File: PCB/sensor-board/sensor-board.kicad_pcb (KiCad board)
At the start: 2 copper layers, 70 x 58 mm, 37 parts, among them J1 SENSOR, Q1 BSS138, Q2 BSS138, Q3 BSS138, Q4 BSS138

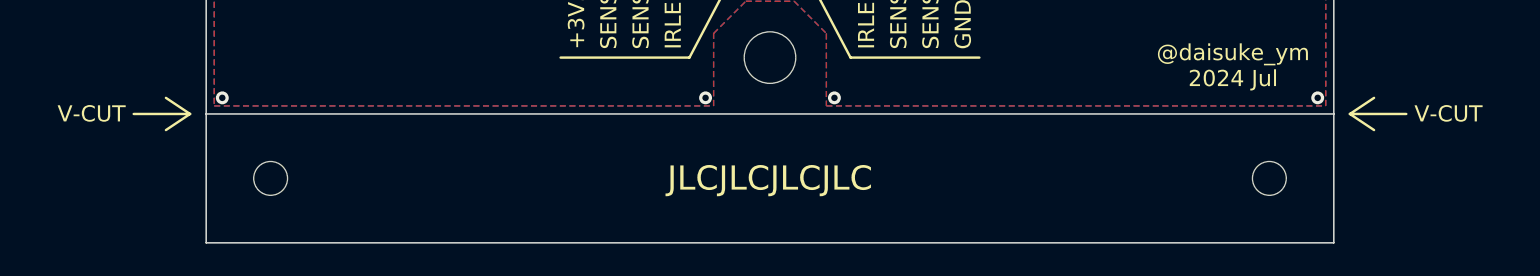
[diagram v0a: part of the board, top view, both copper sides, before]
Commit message: JLCPCB で監査エラー（V-CUTできるサイズを超えているとのこと）が出たので、マウスバイトに変更した。
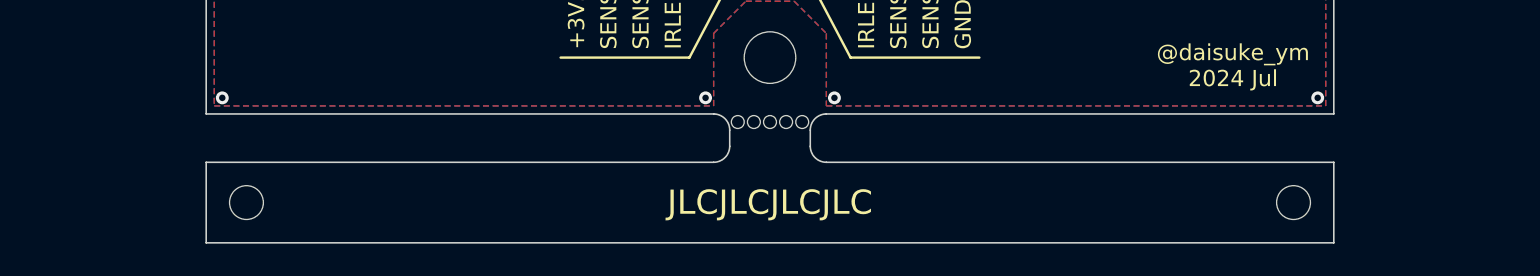
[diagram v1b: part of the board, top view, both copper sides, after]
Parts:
- added CH**: CuttingHole_0.8, MyLib:CuttingHole_0.8, F.Cu at (151.0, 92.5)
- added CH**: CuttingHole_0.8, MyLib:CuttingHole_0.8, F.Cu at (149.0, 92.5)
- added CH**: CuttingHole_0.8, MyLib:CuttingHole_0.8, F.Cu at (148.0, 92.5)
- added CH**: CuttingHole_0.8, MyLib:CuttingHole_0.8, F.Cu at (150.0, 92.5)
- added CH**: CuttingHole_0.8, MyLib:CuttingHole_0.8, F.Cu at (152.0, 92.5)
- moved REF** 2.12 mm to (117.5, 97.5)
- moved REF** 2.12 mm to (182.5, 97.5)
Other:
- outline, holes or cut-outs redrawn
- board text removed: "V-CUT"
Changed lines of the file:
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@@
   )
   (footprint "MountingHole:MountingHole_2.1mm" (layer "F.Cu")
-    (at 119 96)
+    (at 117.5 97.5)
     (descr "Mounting Hole 2.1mm, no annular")
     (tags "mounting hole 2.1mm no annular")
@@
       (rotate (xyz 0 0 0))
     )
+  )
+  (footprint "MyLib:CuttingHole_0.8" (layer "F.Cu")
+    (at 151 92.5)
+    (attr through_hole)
+    (fp_text reference "CH**" (at 0 -2 unlocked) (layer "F.SilkS") hide
+        (effects (font (size 1 1) (thickness 0.1)))
+    )
+    (fp_text value "CuttingHole_0.8" (at 0 2.5 unlocked) (layer "F.Fab") hide
+        (effects (font (size 1 1) (thickness 0.15)))
+    )
+    (fp_text user "${REFERENCE}" (at 0 4 unlocked) (layer "F.Fab") hide
+        (effects (font (size 1 1) (thickness 0.15)))
+    )
+    (pad "" np_thru_hole circle (at 0 0) (size 0.8 0.8) (drill 0.8) (layers "F&B.Cu" "*.Mask"))
   )
   (footprint "MountingHole:MountingHole_3.2mm_M3" (layer "F.Cu")
@@
   )
   (footprint "MountingHole:MountingHole_2.1mm" (layer "F.Cu")
-    (at 181 96)
+    (at 182.5 97.5)
     (descr "Mounting Hole 2.1mm, no annular")
     (tags "mounting hole 2.1mm no annular")
@@
       (rotate (xyz 0 0 0))
     )
+  )
+  (footprint "MyLib:CuttingHole_0.8" (layer "F.Cu")
+    (at 149 92.5)
+    (attr through_hole)
+    (fp_text reference "CH**" (at 0 -2 unlocked) (layer "F.SilkS") hide
+        (effects (font (size 1 1) (thickness 0.1)))
+    )
+    (fp_text value "CuttingHole_0.8" (at 0 2.5 unlocked) (layer "F.Fab") hide
+        (effects (font (size 1 1) (thickness 0.15)))
+    )
+    (fp_text user "${REFERENCE}" (at 0 4 unlocked) (layer "F.Fab") hide
+        (effects (font (size 1 1) (thickness 0.15)))
+    )
+    (pad "" np_thru_hole circle (at 0 0) (size 0.8 0.8) (drill 0.8) (layers "F&B.Cu" "*.Mask"))
+  )
+  (footprint "MyLib:CuttingHole_0.8" (layer "F.Cu")
+    (at 148 92.5)
+    (attr through_hole)
+    (fp_text reference "CH**" (at 0 -2 unlocked) (layer "F.SilkS") hide
+        (effects (font (size 1 1) (thickness 0.1)))
+    )
+    (fp_text value "CuttingHole_0.8" (at 0 2.5 unlocked) (layer "F.Fab") hide
+        (effects (font (size 1 1) (thickness 0.15)))
+    )
+    (fp_text user "${REFERENCE}" (at 0 4 unlocked) (layer "F.Fab") hide
+        (effects (font (size 1 1) (thickness 0.15)))
+    )
+    (pad "" np_thru_hole circle (at 0 0) (size 0.8 0.8) (drill 0.8) (layers "F&B.Cu" "*.Mask"))
   )
   (footprint "Capacitor_SMD:C_0805_2012Metric" (layer "F.Cu")
@@
     )
   )
+  (footprint "MyLib:CuttingHole_0.8" (layer "F.Cu")
+    (at 150 92.5)
+    (attr through_hole)
+    (fp_text reference "CH**" (at 0 -2 unlocked) (layer "F.SilkS") hide
+        (effects (font (size 1 1) (thickness 0.1)))
+    )
+    (fp_text value "CuttingHole_0.8" (at 0 2.5 unlocked) (layer "F.Fab") hide
+        (effects (font (size 1 1) (thickness 0.15)))
+    )
+    (fp_text user "${REFERENCE}" (at 0 4 unlocked) (layer "F.Fab") hide
+        (effects (font (size 1 1) (thickness 0.15)))
+    )
+    (pad "" np_thru_hole circle (at 0 0) (size 0.8 0.8) (drill 0.8) (layers "F&B.Cu" "*.Mask"))
+  )
   (footprint "Resistor_SMD:R_0603_1608Metric" (layer "F.Cu")
     (at 175 70 180)
@@
       (rotate (xyz 0 0 0))
     )
+  )
+  (footprint "MyLib:CuttingHole_0.8" (layer "F.Cu")
+    (at 152 92.5)
+    (attr through_hole)
+    (fp_text reference "CH**" (at 0 -2 unlocked) (layer "F.SilkS") hide
+        (effects (font (size 1 1) (thickness 0.1)))
+    )
+    (fp_text value "CuttingHole_0.8" (at 0 2.5 unlocked) (layer "F.Fab") hide
+        (effects (font (size 1 1) (thickness 0.15)))
+    )
+    (fp_text user "${REFERENCE}" (at 0 4 unlocked) (layer "F.Fab") hide
+        (effects (font (size 1 1) (thickness 0.15)))
+    )
+    (pad "" np_thru_hole circle (at 0 0) (size 0.8 0.8) (drill 0.8) (layers "F&B.Cu" "*.Mask"))
   )
   (footprint "MountingHole:MountingHole_3.2mm_M3" (layer "F.Cu")
@@
   (gr_line (start 150 79) (end 145 88.5)
     (stroke (width 0.15) (type default)) (layer "B.SilkS"))
-  (gr_line (start 110.5 92) (end 114 92)
-    (stroke (width 0.15) (type default)) (layer "F.SilkS"))
-  (gr_line (start 186 92) (end 187.5 91)
-    (stroke (width 0.15) (type default)) (layer "F.SilkS"))
-  (gr_line (start 186 92) (end 187.5 93)
-    (stroke (width 0.15) (type default)) (layer "F.SilkS"))
-  (gr_line (start 189.5 92) (end 186 92)
-    (stroke (width 0.15) (type default)) (layer "F.SilkS"))
-  (gr_line (start 114 92) (end 112.5 91)
-    (stroke (width 0.15) (type default)) (layer "F.SilkS"))
   (gr_line (start 163 88.5) (end 155 88.5)
     (stroke (width 0.15) (type default)) (layer "F.SilkS"))
@@
   (gr_line (start 145 88.5) (end 150 79)
     (stroke (width 0.15) (type default)) (layer "F.SilkS"))
-  (gr_line (start 114 92) (end 112.5 93)
-    (stroke (width 0.15) (type default)) (layer "F.SilkS"))
+  (gr_arc (start 147.5 94) (mid 147.207107 94.707107) (end 146.5 95)
+    (stroke (width 0.1) (type default)) (layer "Edge.Cuts"))
   (gr_line (start 142 42) (end 142 63)
     (stroke (width 0.1) (type default)) (layer "Edge.Cuts"))
+  (gr_line (start 146.5 95) (end 115 95)
+    (stroke (width 0.1) (type default)) (layer "Edge.Cuts"))
   (gr_arc (start 158 63) (mid 157.707107 63.707107) (end 157 64)
     (stroke (width 0.1) (type default)) (layer "Edge.Cuts"))
@@
   (gr_line (start 143 64) (end 157 64)
     (stroke (width 0.1) (type default)) (layer "Edge.Cuts"))
-  (gr_line (start 115 92) (end 115 100)
+  (gr_line (start 147.5 94) (end 147.5 93)
+    (stroke (width 0.1) (type default)) (layer "Edge.Cuts"))
+  (gr_arc (start 146.5 92) (mid 147.207107 92.292893) (end 147.5 93)
+    (stroke (width 0.1) (type default)) (layer "Edge.Cuts"))
+  (gr_line (start 115 95) (end 115 100)
+    (stroke (width 0.1) (type default)) (layer "Edge.Cuts"))
+  (gr_line (start 185 95) (end 153.5 95)
+    (stroke (width 0.1) (type default)) (layer "Edge.Cuts"))
+  (gr_arc (start 153.5 95) (mid 152.792893 94.707107) (end 152.5 94)
     (stroke (width 0.1) (type default)) (layer "Edge.Cuts"))
   (gr_arc (start 115 53.064029) (mid 127.800855 45.825864) (end 142 42)
@@
   (gr_arc (start 143 64) (mid 142.292893 63.707107) (end 142 63)
     (stroke (width 0.1) (type default)) (layer "Edge.Cuts"))
-  (gr_line (start 115 92) (end 185 92)
+  (gr_line (start 115 92) (end 146.5 92)
     (stroke (width 0.1) (type default)) (layer "Edge.Cuts"))
   (gr_line (start 115 53.064029) (end 115 92)
     (stroke (width 0.1) (type default)) (layer "Edge.Cuts"))
+  (gr_arc (start 152.5 93) (mid 152.792893 92.292893) (end 153.5 92)
+    (stroke (width 0.1) (type default)) (layer "Edge.Cuts"))
   (gr_line (start 158 63) (end 158 42)
     (stroke (width 0.1) (type default)) (layer "Edge.Cuts"))
@@
   (gr_line (start 115 100) (end 185 100)
     (stroke (width 0.1) (type default)) (layer "Edge.Cuts"))
-  (gr_line (start 185 100) (end 185 92)
+  (gr_line (start 152.5 94) (end 152.5 93)
+    (stroke (width 0.1) (type default)) (layer "Edge.Cuts"))
+  (gr_line (start 153.5 92) (end 185 92)
+    (stroke (width 0.1) (type default)) (layer "Edge.Cuts"))
+  (gr_line (start 185 100) (end 185 95)
     (stroke (width 0.1) (type default)) (layer "Edge.Cuts"))
   (gr_line (start 137 54) (end 137 37)
@@
     (effects (font (size 1 1) (thickness 0.15)) (justify left))
   )
-  (gr_text "V-CUT" (at 190 92) (layer "F.SilkS")
-    (effects (font (size 1 1) (thickness 0.15)) (justify left))
-  )
   (gr_text "@daisuke_ym\n2024 Jul" (at 178.75 89) (layer "F.SilkS")
     (effects (font (size 1 1) (thickness 0.15)))
   )
-  (gr_text "JLCJLCJLCJLC" (at 150 96) (layer "F.SilkS")
+  (gr_text "JLCJLCJLCJLC" (at 150 97.5) (layer "F.SilkS")
     (effects (font (size 1.5 1.5) (thickness 0.15)))
   )
@@
     (effects (font (size 1 1) (thickness 0.15)) (justify left bottom))
   )
-  (gr_text "V-CUT" (at 110 92) (layer "F.SilkS")
-    (effects (font (size 1 1) (thickness 0.15)) (justify right))
-  )
   (gr_text "GND" (at 162 88 90) (layer "F.SilkS")
